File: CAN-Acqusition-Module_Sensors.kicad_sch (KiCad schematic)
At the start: 0 parts

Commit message: Added analog and sensors sections
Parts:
- added C? (x2): 100 nF, Capacitor_SMD:C_0402_1005Metric, symbol Device:C_Small
- added C? (x2): 1 uF, Capacitor_SMD:C_0603_1608Metric, symbol Device:C_Small
- added C?: 10 uF, Capacitor_SMD:C_1206_3216Metric, symbol Device:C_Small
- added D? (x2): CM1213A-01SO, Package_TO_SOT_SMD:SOT-23, symbol Power_Protection:CM1213A-01SO
- added R? (x6): Ω, Resistor_SMD:R_0603_1608Metric, symbol Device:R_Small_US
- added R? (x2): 1.1 kΩ, Resistor_SMD:R_0603_1608Metric, symbol Device:R_Small_US
- added R? (x2): 0 Ω, Resistor_SMD:R_0603_1608Metric, symbol Device:R_Small_US
- added R?: 10 kΩ, Resistor_SMD:R_0603_1608Metric, symbol Device:R_Small_US
- added U?: SCD30, CAN-Acquisition-Module:SCD30, symbol CAN-Acquisition-Module:SCD30
- added U?: SHT35-DIS, Sensor_Humidity:Sensirion_DFN-8-1EP_2.5x2.5mm_P0.5mm_EP1.1x1.7mm, symbol Sensor_Humidity:SHT35-DIS
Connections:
- new net: R?.1, U?.6 (PWM)
- new net: R?.1, U?.3 (ALERT)
- new net: R?.1, U?.5 (RDY)
- new net: R?.1, R?.2, U?.7 (SEL)
- new net: R?.1, R?.2, U?.2 (ADDR)
- new net: R?.1, R?.2, U?.6 (~{RESET})
- new net +3V3: C?.1, C?.1, C?.1, C?.1, C?.1, R?.1, R?.1, R?.1, R?.1, R?.1, U?.1 (VDD), U?.5 (VDD)
- new net CO2_PWM: R?.2
- new net CO2_RDY: R?.2
- new net GND: C?.2, C?.2, C?.2, C?.2, C?.2, R?.2, R?.2, U?.2 (GND), U?.7 (R), U?.8 (VSS), U?.9 (VSS)
- new net HUMIDITY_ALERT: R?.2
- new net HUMIDITY_RESET: R?.2
- new net I2C_SCL: D?.1 (CH1), R?.2, U?.3 (TX/SCL), U?.4 (SCL)
- new net I2C_SDA: D?.1 (CH1), R?.2, U?.1 (SDA), U?.4 (RX/SDA)
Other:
- note added: "80 Hz"
- note added: "Place TVSs near exposed I2C connector"
- note added: "Standard-mode, 50 kbit/s w/ clock stretching as per Sensirion guide"
- company: (none) -> École de Technologie Supérieure - Laboratoire thermique et science du bâtiment (LTSB)
- title: (none) -> CANbus Acquisition Module

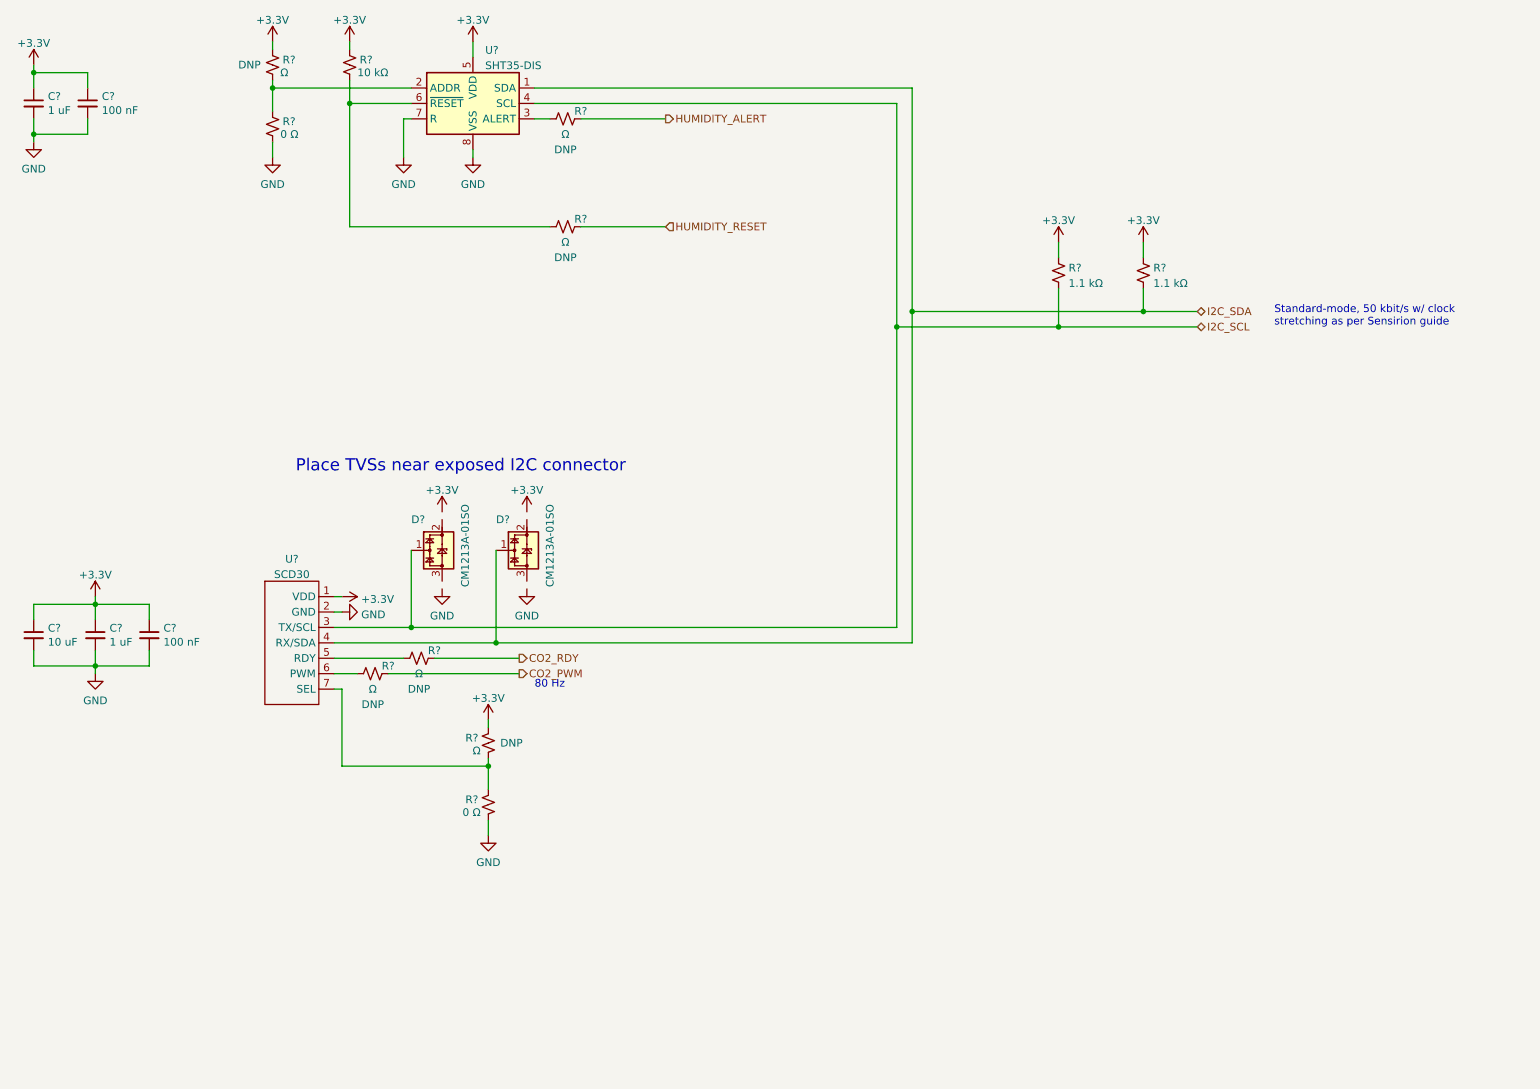
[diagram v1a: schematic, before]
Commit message: Added screen sections and annotations
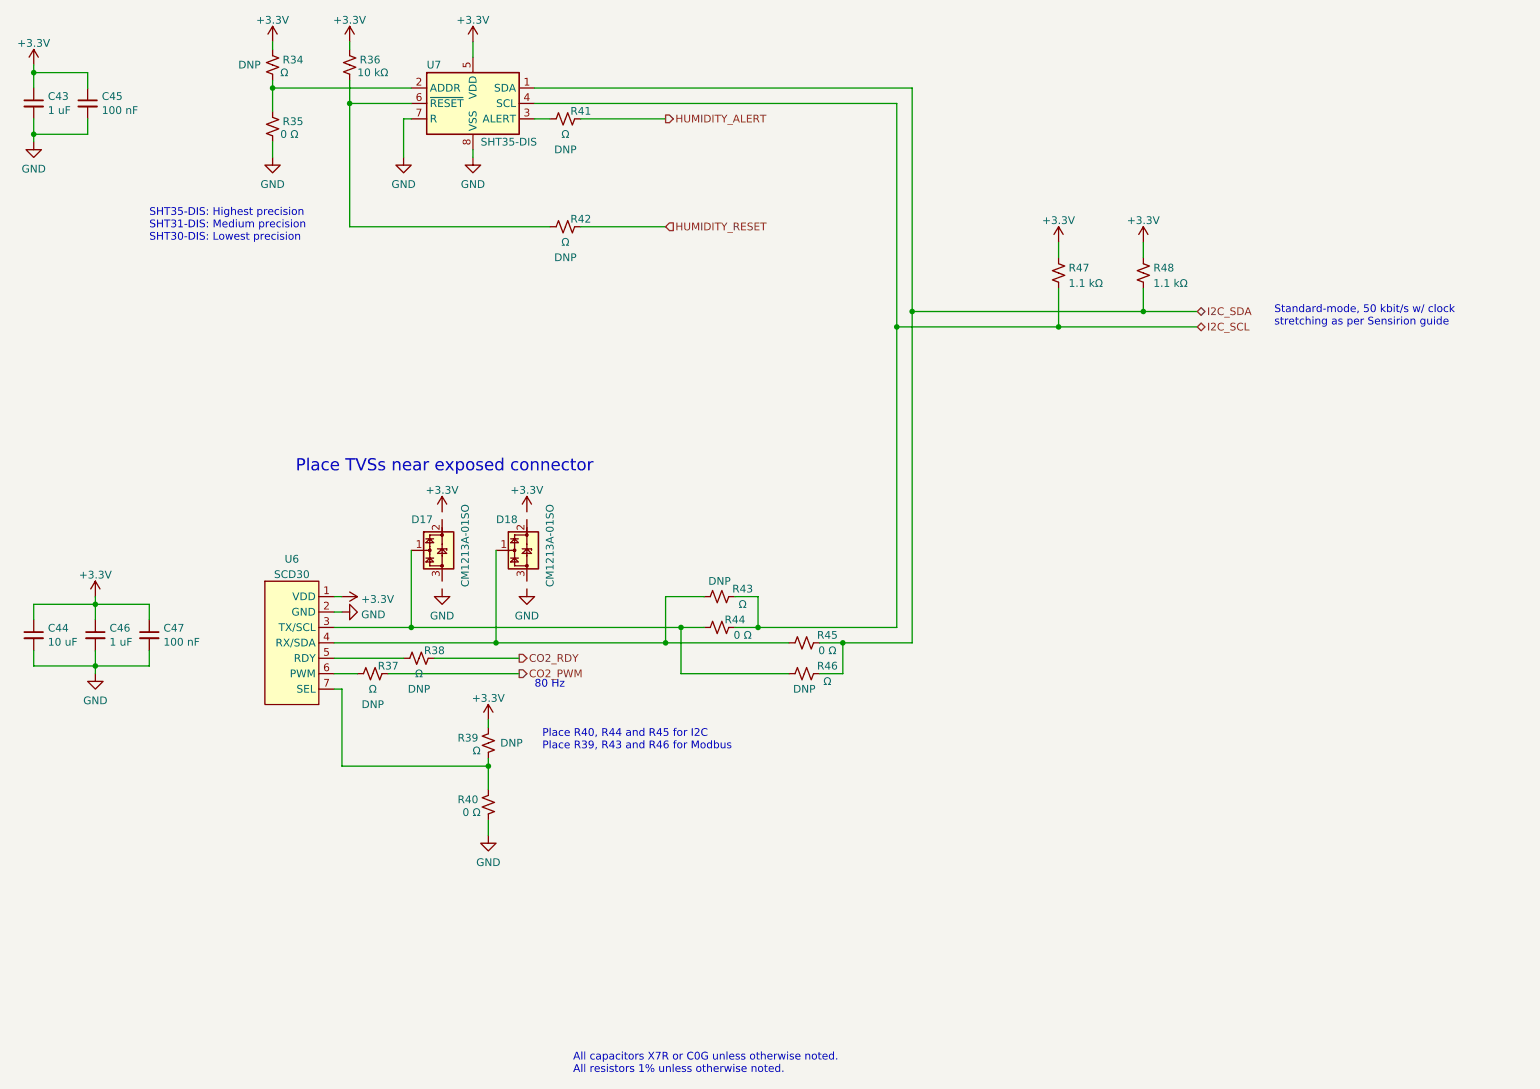
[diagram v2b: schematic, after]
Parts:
- removed U?: SCD30, CAN-Acquisition-Module:SCD30, symbol CAN-Acquisition-Module:SCD30
- added R43, R46: Ω, Resistor_SMD:R_0603_1608Metric, symbol Device:R_Small_US
- added R44, R45: 0 Ω, Resistor_SMD:R_0603_1608Metric, symbol Device:R_Small_US
- added U6: SCD30, CAN-Acquisition-Module:SCD30, symbol CAN-Acquisition-Module:SCD30
- C43, C46: renamed from C?; Mfr. (none) -> Samsung Electro-Mechanics; P/N (none) -> CL10B105KA8NNNC; Rated Voltage (none) -> 25V
- C44: renamed from C?; footprint Capacitor_SMD:C_1206_3216Metric -> Capacitor_SMD:C_0805_2012Metric; Mfr. (none) -> TDK Corporation; P/N (none) -> C2012X7R0J106K125AB; Rated Voltage (none) -> 6.3V
- C45, C47: renamed from C?; Mfr. (none) -> KYOCERA AVX; P/N (none) -> 0402YC104KAT2A; Rated Voltage (none) -> 16V
- U7: renamed from U?; footprint Sensor_Humidity:Sensirion_DFN-8-1EP_2.5x2.5mm_P0.5mm_EP1.1x1.7mm -> CAN-Acquisition-Module:Sensirion_DFN-8-1EP_2.5x2.5mm_P0.5mm_EP1.1x1.7mm
- gave numbers to parts that had none: 13
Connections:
- net +3V3: now also U6.1 (VDD)
- net GND: now also U6.2 (GND)
- net I2C_SCL: now also R43.2, R44.2; no longer D17.1 (CH1)
- net I2C_SDA: now also R45.2, R46.2; no longer D18.1 (CH1)
- net at R37.1: now also U6.6 (PWM)
- net at R38.1: now also U6.5 (RDY)
- net at R39.2, R40.1: now also U6.7 (SEL)
- new net: D18.1 (CH1), R43.1, R45.1, U6.4 (RX/SDA)
- new net: D17.1 (CH1), R44.1, R46.1, U6.3 (TX/SCL)
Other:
- note added: "All capacitors X7R or C0G unless otherwise noted. All resistors 1% unless otherwise noted."
- note added: "Place R40, R44 and R45 for I2C Place R39, R43 and R46 for Modbus"
- note added: "Place TVSs near exposed connector"
- note added: "SHT35-DIS: Highest precision SHT31-DIS: Medium precision SHT30-DIS: Lowest precision"
- note removed: "Place TVSs near exposed I2C connector"

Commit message: PCB started
Placement well advanced
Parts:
- removed C43: 1 uF, Capacitor_SMD:C_0603_1608Metric, symbol Device:C_Small
- removed C45: 100 nF, Capacitor_SMD:C_0402_1005Metric, symbol Device:C_Small
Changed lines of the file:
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@@
     (comment 1 "Designer: Hugo Boyce")
   )
-  (junction (at 36.83 29.21) (diameter 0) (color 0 0 0 0)
-  )
   (junction (at 179.07 71.12) (diameter 0) (color 0 0 0 0)
   )
-  (junction (at 36.83 39.37) (diameter 0) (color 0 0 0 0)
-  )
   (junction (at 46.99 116.84) (diameter 0) (color 0 0 0 0)
   )
@@
     (stroke (width 0) (type default) (color 0 0 0 0))
   )
-  (wire (pts (xy 45.72 39.37) (xy 45.72 36.83))
-    (stroke (width 0) (type default) (color 0 0 0 0))
-  )
   (wire (pts (xy 179.07 71.12) (xy 205.74 71.12))
     (stroke (width 0) (type default) (color 0 0 0 0))
@@
     (stroke (width 0) (type default) (color 0 0 0 0))
   )
-  (wire (pts (xy 36.83 39.37) (xy 36.83 36.83))
-    (stroke (width 0) (type default) (color 0 0 0 0))
-  )
   (wire (pts (xy 111.76 143.51) (xy 111.76 147.32))
     (stroke (width 0) (type default) (color 0 0 0 0))
@@
     (stroke (width 0) (type default) (color 0 0 0 0))
   )
-  (wire (pts (xy 36.83 39.37) (xy 45.72 39.37))
-    (stroke (width 0) (type default) (color 0 0 0 0))
-  )
   (wire (pts (xy 170.18 123.19) (xy 181.61 123.19))
     (stroke (width 0) (type default) (color 0 0 0 0))
   )
-  (wire (pts (xy 36.83 39.37) (xy 36.83 40.64))
-    (stroke (width 0) (type default) (color 0 0 0 0))
-  )
   (wire (pts (xy 99.06 120.65) (xy 143.51 120.65))
     (stroke (width 0) (type default) (color 0 0 0 0))
@@
     (stroke (width 0) (type default) (color 0 0 0 0))
   )
-  (wire (pts (xy 45.72 31.75) (xy 45.72 29.21))
-    (stroke (width 0) (type default) (color 0 0 0 0))
-  )
   (wire (pts (xy 36.83 116.84) (xy 46.99 116.84))
     (stroke (width 0) (type default) (color 0 0 0 0))
@@
     (stroke (width 0) (type default) (color 0 0 0 0))
   )
-  (wire (pts (xy 36.83 31.75) (xy 36.83 29.21))
-    (stroke (width 0) (type default) (color 0 0 0 0))
-  )
   (wire (pts (xy 181.61 68.58) (xy 219.71 68.58))
     (stroke (width 0) (type default) (color 0 0 0 0))
@@
     (stroke (width 0) (type default) (color 0 0 0 0))
   )
-  (wire (pts (xy 45.72 29.21) (xy 36.83 29.21))
-    (stroke (width 0) (type default) (color 0 0 0 0))
-  )
   (wire (pts (xy 55.88 119.38) (xy 55.88 116.84))
     (stroke (width 0) (type default) (color 0 0 0 0))
@@
   )
   (wire (pts (xy 109.22 41.91) (xy 109.22 43.18))
-    (stroke (width 0) (type default) (color 0 0 0 0))
-  )
-  (wire (pts (xy 36.83 27.94) (xy 36.83 29.21))
     (stroke (width 0) (type default) (color 0 0 0 0))
   )
@@
     (pin "2")
     (pin "3")
-  )
-  (symbol (lib_id "power:+3.3V") (at 36.83 27.94 0) (unit 1)
-    (in_bom yes) (on_board yes) (fields_autoplaced)
-    (property "Reference" "#PWR0108" (id 0) (at 36.83 31.75 0)
-      (effects (font (size 1.27 1.27)) hide)
-    )
-    (property "Value" "+3.3V" (id 1) (at 36.83 24.3642 0))
-    (property "Footprint" "" (id 2) (at 36.83 27.94 0)
-      (effects (font (size 1.27 1.27)) hide)
-    )
-    (property "Datasheet" "" (id 3) (at 36.83 27.94 0)
-      (effects (font (size 1.27 1.27)) hide)
-    )
-    (pin "1")
   )
   (symbol (lib_id "Device:R_Small_US") (at 163.83 123.19 90) (unit 1)
@@
     )
     (pin "1")
-  )
-  (symbol (lib_id "Device:C_Small") (at 36.83 34.29 0) (unit 1)
-    (in_bom yes) (on_board yes)
-    (property "Reference" "C43" (id 0) (at 39.1668 33.1216 0)
-      (effects (font (size 1.27 1.27)) (justify left))
-    )
-    (property "Value" "1 uF" (id 1) (at 39.1668 35.433 0)
-      (effects (font (size 1.27 1.27)) (justify left))
-    )
-    (property "Footprint" "Capacitor_SMD:C_0603_1608Metric" (id 2) (at 36.83 34.29 0)
-      (effects (font (size 1.27 1.27)) hide)
-    )
-    (property "Datasheet" "~" (id 3) (at 36.83 34.29 0)
-      (effects (font (size 1.27 1.27)) hide)
-    )
-    (property "Mfr." "Samsung Electro-Mechanics " (id 4) (at 36.83 34.29 0)
-      (effects (font (size 1.27 1.27)) hide)
-    )
-    (property "P/N" "CL10B105KA8NNNC" (id 5) (at 36.83 34.29 0)
-      (effects (font (size 1.27 1.27)) hide)
-    )
-    (property "Rated Voltage" "25V" (id 6) (at 36.83 34.29 0)
-      (effects (font (size 1.27 1.27)) hide)
-    )
-    (pin "1")
-    (pin "2")
   )
   (symbol (lib_id "power:GND") (at 118.11 114.3 0) (unit 1)
@@
     (pin "1")
   )
-  (symbol (lib_id "power:GND") (at 36.83 40.64 0) (unit 1)
-    (in_bom yes) (on_board yes) (fields_autoplaced)
-    (property "Reference" "#PWR0109" (id 0) (at 36.83 46.99 0)
-      (effects (font (size 1.27 1.27)) hide)
-    )
-    (property "Value" "GND" (id 1) (at 36.83 45.0834 0))
-    (property "Footprint" "" (id 2) (at 36.83 40.64 0)
-      (effects (font (size 1.27 1.27)) hide)
-    )
-    (property "Datasheet" "" (id 3) (at 36.83 40.64 0)
-      (effects (font (size 1.27 1.27)) hide)
-    )
-    (pin "1")
-  )
   (symbol (lib_id "power:+3.3V") (at 76.2 24.13 0) (unit 1)
     (in_bom yes) (on_board yes) (fields_autoplaced)
@@
     (pin "1")
   )
-  (symbol (lib_id "Device:C_Small") (at 45.72 34.29 0) (unit 1)
-    (in_bom yes) (on_board yes)
-    (property "Reference" "C45" (id 0) (at 48.0568 33.1216 0)
-      (effects (font (size 1.27 1.27)) (justify left))
-    )
-    (property "Value" "100 nF" (id 1) (at 48.0568 35.433 0)
-      (effects (font (size 1.27 1.27)) (justify left))
-    )
-    (property "Footprint" "Capacitor_SMD:C_0402_1005Metric" (id 2) (at 45.72 34.29 0)
-      (effects (font (size 1.27 1.27)) hide)
-    )
-    (property "Datasheet" "~" (id 3) (at 45.72 34.29 0)
-      (effects (font (size 1.27 1.27)) hide)
-    )
-    (property "Mfr." "KYOCERA AVX " (id 4) (at 45.72 34.29 0)
-      (effects (font (size 1.27 1.27)) hide)
-    )
-    (property "P/N" "0402YC104KAT2A" (id 5) (at 45.72 34.29 0)
-      (effects (font (size 1.27 1.27)) hide)
-    )
-    (property "Rated Voltage" "16V" (id 6) (at 45.72 34.29 0)
-      (effects (font (size 1.27 1.27)) hide)
-    )
-    (pin "1")
-    (pin "2")
-  )
   (symbol (lib_id "power:+3.3V") (at 205.74 57.15 0) (unit 1)

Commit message: Layout of analog section started
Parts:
- renumbered C44 to C47, C46 to C48, C47 to C49
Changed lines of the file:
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@@
   (symbol (lib_id "power:+3.3V") (at 109.22 24.13 0) (unit 1)
     (in_bom yes) (on_board yes) (fields_autoplaced)
-    (property "Reference" "#PWR0120" (id 0) (at 109.22 27.94 0)
+    (property "Reference" "#PWR0124" (id 0) (at 109.22 27.94 0)
       (effects (font (size 1.27 1.27)) hide)
     )
@@
   (symbol (lib_id "power:GND") (at 87.63 118.11 90) (unit 1)
     (in_bom yes) (on_board yes) (fields_autoplaced)
-    (property "Reference" "#PWR0115" (id 0) (at 93.98 118.11 0)
+    (property "Reference" "#PWR0119" (id 0) (at 93.98 118.11 0)
       (effects (font (size 1.27 1.27)) hide)
     )
@@
   (symbol (lib_id "Device:C_Small") (at 55.88 121.92 0) (unit 1)
     (in_bom yes) (on_board yes)
-    (property "Reference" "C47" (id 0) (at 58.2168 120.7516 0)
+    (property "Reference" "C49" (id 0) (at 58.2168 120.7516 0)
       (effects (font (size 1.27 1.27)) (justify left))
     )
@@
   (symbol (lib_id "power:GND") (at 111.76 154.94 0) (mirror y) (unit 1)
     (in_bom yes) (on_board yes) (fields_autoplaced)
-    (property "Reference" "#PWR0123" (id 0) (at 111.76 161.29 0)
+    (property "Reference" "#PWR0127" (id 0) (at 111.76 161.29 0)
       (effects (font (size 1.27 1.27)) hide)
     )
@@
   (symbol (lib_id "power:GND") (at 76.2 43.18 0) (unit 1)
     (in_bom yes) (on_board yes) (fields_autoplaced)
-    (property "Reference" "#PWR0113" (id 0) (at 76.2 49.53 0)
+    (property "Reference" "#PWR0117" (id 0) (at 76.2 49.53 0)
       (effects (font (size 1.27 1.27)) hide)
     )
@@
   (symbol (lib_id "power:GND") (at 109.22 43.18 0) (unit 1)
     (in_bom yes) (on_board yes) (fields_autoplaced)
-    (property "Reference" "#PWR0121" (id 0) (at 109.22 49.53 0)
+    (property "Reference" "#PWR0125" (id 0) (at 109.22 49.53 0)
       (effects (font (size 1.27 1.27)) hide)
     )
@@
   (symbol (lib_id "power:+3.3V") (at 219.71 57.15 0) (unit 1)
     (in_bom yes) (on_board yes) (fields_autoplaced)
-    (property "Reference" "#PWR0127" (id 0) (at 219.71 60.96 0)
+    (property "Reference" "#PWR0131" (id 0) (at 219.71 60.96 0)
       (effects (font (size 1.27 1.27)) hide)
     )
@@
   (symbol (lib_id "power:GND") (at 46.99 128.27 0) (unit 1)
     (in_bom yes) (on_board yes) (fields_autoplaced)
-    (property "Reference" "#PWR0111" (id 0) (at 46.99 134.62 0)
+    (property "Reference" "#PWR0115" (id 0) (at 46.99 134.62 0)
       (effects (font (size 1.27 1.27)) hide)
     )
@@
   (symbol (lib_id "power:GND") (at 118.11 114.3 0) (unit 1)
     (in_bom yes) (on_board yes) (fields_autoplaced)
-    (property "Reference" "#PWR0125" (id 0) (at 118.11 120.65 0)
+    (property "Reference" "#PWR0129" (id 0) (at 118.11 120.65 0)
       (effects (font (size 1.27 1.27)) hide)
     )
@@
   (symbol (lib_id "Device:C_Small") (at 36.83 121.92 0) (unit 1)
     (in_bom yes) (on_board yes)
-    (property "Reference" "C44" (id 0) (at 39.1668 120.7516 0)
+    (property "Reference" "C47" (id 0) (at 39.1668 120.7516 0)
       (effects (font (size 1.27 1.27)) (justify left))
     )
@@
   (symbol (lib_id "Device:C_Small") (at 46.99 121.92 0) (unit 1)
     (in_bom yes) (on_board yes)
-    (property "Reference" "C46" (id 0) (at 49.3268 120.7516 0)
+    (property "Reference" "C48" (id 0) (at 49.3268 120.7516 0)
       (effects (font (size 1.27 1.27)) (justify left))
     )
@@
   (symbol (lib_id "power:GND") (at 104.14 114.3 0) (unit 1)
     (in_bom yes) (on_board yes) (fields_autoplaced)
-    (property "Reference" "#PWR0119" (id 0) (at 104.14 120.65 0)
+    (property "Reference" "#PWR0123" (id 0) (at 104.14 120.65 0)
       (effects (font (size 1.27 1.27)) hide)
     )
@@
   (symbol (lib_id "power:+3.3V") (at 111.76 135.89 0) (mirror y) (unit 1)
     (in_bom yes) (on_board yes) (fields_autoplaced)
-    (property "Reference" "#PWR0122" (id 0) (at 111.76 139.7 0)
+    (property "Reference" "#PWR0126" (id 0) (at 111.76 139.7 0)
       (effects (font (size 1.27 1.27)) hide)
     )
@@
   (symbol (lib_id "power:+3.3V") (at 104.14 101.6 0) (unit 1)
     (in_bom yes) (on_board yes) (fields_autoplaced)
-    (property "Reference" "#PWR0118" (id 0) (at 104.14 105.41 0)
+    (property "Reference" "#PWR0122" (id 0) (at 104.14 105.41 0)
       (effects (font (size 1.27 1.27)) hide)
     )
@@
   (symbol (lib_id "power:+3.3V") (at 118.11 101.6 0) (unit 1)
     (in_bom yes) (on_board yes) (fields_autoplaced)
-    (property "Reference" "#PWR0124" (id 0) (at 118.11 105.41 0)
+    (property "Reference" "#PWR0128" (id 0) (at 118.11 105.41 0)
       (effects (font (size 1.27 1.27)) hide)
     )
@@
   (symbol (lib_id "power:+3.3V") (at 76.2 24.13 0) (unit 1)
     (in_bom yes) (on_board yes) (fields_autoplaced)
-    (property "Reference" "#PWR0112" (id 0) (at 76.2 27.94 0)
+    (property "Reference" "#PWR0116" (id 0) (at 76.2 27.94 0)
       (effects (font (size 1.27 1.27)) hide)
     )
@@
   (symbol (lib_id "power:+3.3V") (at 87.63 115.57 270) (unit 1)
     (in_bom yes) (on_board yes) (fields_autoplaced)
-    (property "Reference" "#PWR0114" (id 0) (at 83.82 115.57 0)
+    (property "Reference" "#PWR0118" (id 0) (at 83.82 115.57 0)
       (effects (font (size 1.27 1.27)) hide)
     )
@@
   (symbol (lib_id "power:+3.3V") (at 88.9 24.13 0) (unit 1)
     (in_bom yes) (on_board yes) (fields_autoplaced)
-    (property "Reference" "#PWR0116" (id 0) (at 88.9 27.94 0)
+    (property "Reference" "#PWR0120" (id 0) (at 88.9 27.94 0)
       (effects (font (size 1.27 1.27)) hide)
     )
@@
   (symbol (lib_id "power:GND") (at 97.79 43.18 0) (unit 1)
     (in_bom yes) (on_board yes) (fields_autoplaced)
-    (property "Reference" "#PWR0117" (id 0) (at 97.79 49.53 0)
+    (property "Reference" "#PWR0121" (id 0) (at 97.79 49.53 0)
       (effects (font (size 1.27 1.27)) hide)
     )
@@
   (symbol (lib_id "power:+3.3V") (at 46.99 115.57 0) (unit 1)
     (in_bom yes) (on_board yes) (fields_autoplaced)
-    (property "Reference" "#PWR0110" (id 0) (at 46.99 119.38 0)
+    (property "Reference" "#PWR0114" (id 0) (at 46.99 119.38 0)
       (effects (font (size 1.27 1.27)) hide)
     )
@@
   (symbol (lib_id "power:+3.3V") (at 205.74 57.15 0) (unit 1)
     (in_bom yes) (on_board yes) (fields_autoplaced)
-    (property "Reference" "#PWR0126" (id 0) (at 205.74 60.96 0)
-      (effects (font (size 1.27 1.27)) hide)
-    )
+    (property "Reference" "#PWR0130" (id 0) (at 205.74 60.96 0)
+      (effects (font (size 1.27 1.27)) hide)
+    )
